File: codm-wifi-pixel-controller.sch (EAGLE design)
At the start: 20 parts, among them U1 ESP-WROOM-02, U2 AP2112K, U3 SN74AHCT125D

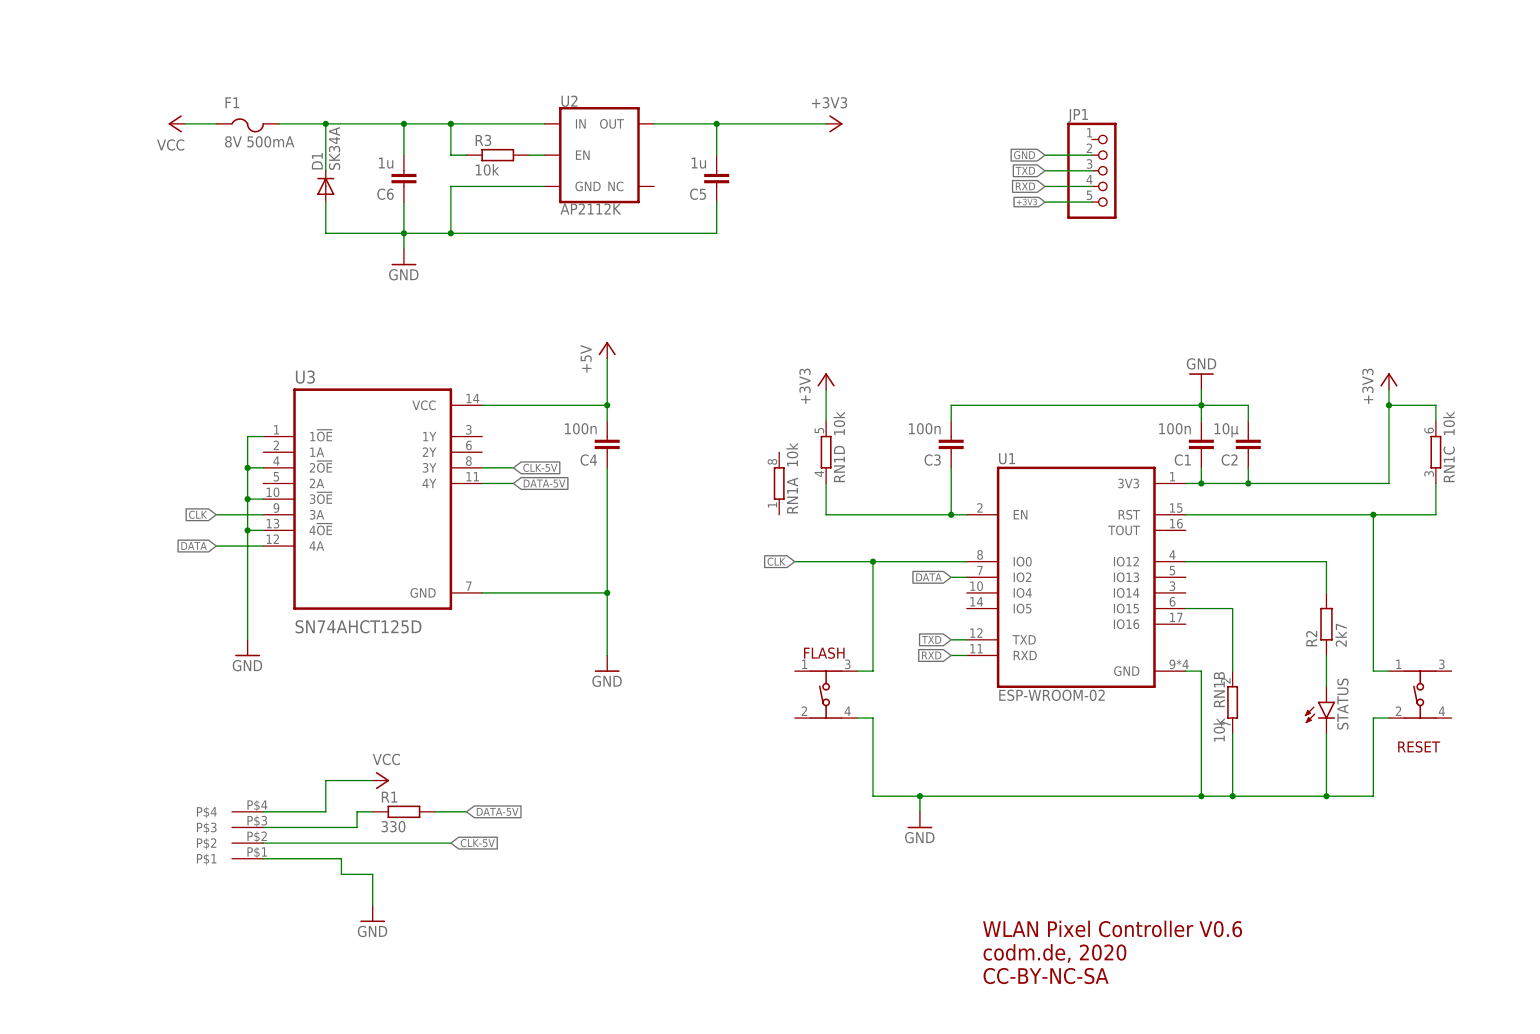
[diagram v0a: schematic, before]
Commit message: version with TLV767 and bigger thermal via/planes
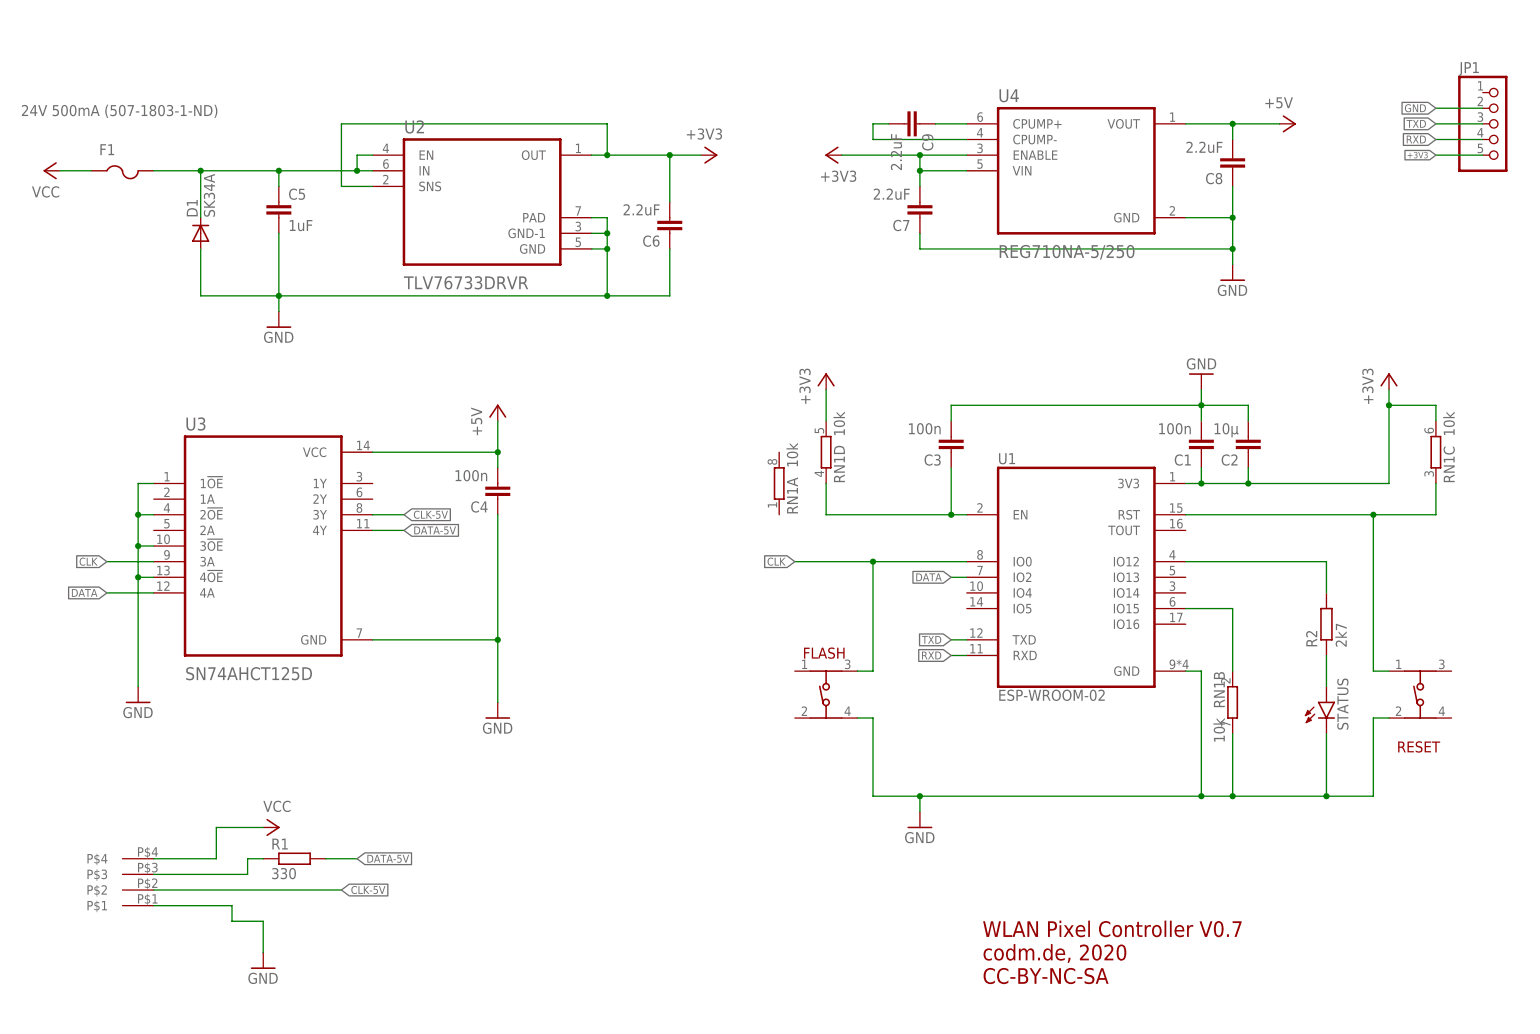
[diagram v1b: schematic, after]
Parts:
- removed R3: 10k, rcl:R-EU_R0805
- added C7, C8, C9: 2.2uF, rcl:C-EUC0603
- added U4: REG710NA-5/250, REG710NA-5_250:REG710NA-5/250
- C1, C2, C3, C4: device rcl:C-EUC0805 -> rcl:C-EUC0603
- C5: value 1u -> 1uF; device rcl:C-EUC0805 -> rcl:C-EUC0603
- C6: value 1u -> 2.2uF; device rcl:C-EUC0805 -> rcl:C-EUC0603
- F1: value 8V 500mA -> 24V 500mA (507-1803-1-ND)
- R1, R2: device rcl:R-EU_R0805 -> rcl:R-EU_R0603
- U2: value AP2112K -> TLV76733DRVR; device SparkFun-IC-Power:V_REG_AP2112K-3.3V -> TLV76733DRVR:TLV76733DRVR
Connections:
- new net N$3: C9.2, U4.CPUMP-
- new net VCCF: C5.1, D1.C, F1.2, U2.EN, U2.IN
- net +3V3: now also C6.2, C7.2, U2.SNS, U4.ENABLE, U4.VIN; no longer C5.2
- net +5V: now also C8.2, U4.VOUT; no longer C6.2, D1.C, F1.2, R3.1, U2.IN
- net GND: now also C5.2, C7.1, C8.1, U2.GND-1, U2.PAD, U4.GND; no longer C5.1
- net N$1: now also C9.1, U4.CPUMP+; no longer R3.2, U2.EN
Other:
- note added: "WLAN Pixel Controller V0.7 codm.de, 2020 CC-BY-NC-SA"
- note removed: "WLAN Pixel Controller V0.6 codm.de, 2020 CC-BY-NC-SA"
- moved on the sheet: C4, C5, C6, D1, F1, JP1, R1, U3

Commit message: prototype 0.7.2
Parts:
- added C10: 100n, rcl:C-EUC0603K
- added EN-2ND: (no value), jumper:SJ
- added R3: 330, rcl:R-EU_R0603
- added TP1, TP2, TP3, TP4, TP5, TP6, TP7, TP8, TP9: PTR1TP14R, testpad:PTR1TP14R
- C1, C2, C3, C7, C8, C9: device rcl:C-EUC0603 -> rcl:C-EUC0603K
- C4: value 100n -> 10u; device rcl:C-EUC0603 -> rcl:C-EUC0805
- C5: value 1uF -> 10uF/16V; device rcl:C-EUC0603 -> rcl:C-EUC0805K
- C6: value 2.2uF -> 100n; device rcl:C-EUC0603 -> rcl:C-EUC0603K
- U2: value TLV76733DRVR -> TLV1117LV33DCYR; device TLV76733DRVR:TLV76733DRVR -> TLV1117LV33DCYR:TLV1117LV33DCYR
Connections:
- net CLK-5V renamed CLK1-5V
- net DATA-5V renamed DATA1-5V
- new net CLK2-5V: TP9.TP, U3.1Y
- new net DATA2-5V: R3.2, U3.2Y
- new net DATA2-5VR: R3.1, TP8.TP
- new net IO13: TP5.TP, U1.IO13
- new net IO14: TP6.TP, U1.IO14
- new net IO16: U1.IO16, U3.1A
- new net IO4: TP3.TP, U1.IO4
- new net IO5: TP4.TP, U1.IO5
- new net N$4: EN-2ND.2, U3.1!OE, U3.2!OE
- net +3V3: now also C4.2, TP2.TP, U2.OUT_2, U2.OUT_4; no longer U2.OUT, U2.SNS
- net +5V: now also C10.2; no longer C4.2
- net GND: now also C10.1, EN-2ND.1, TP1.TP, TP7.TP; no longer U2.GND-1, U2.PAD, U3.1!OE, U3.2!OE
- net TXD: now also U3.2A
- net VCCF: no longer U2.EN
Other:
- note added: "478-3040-1-ND"
- moved on the sheet: C4, C6, RN1B

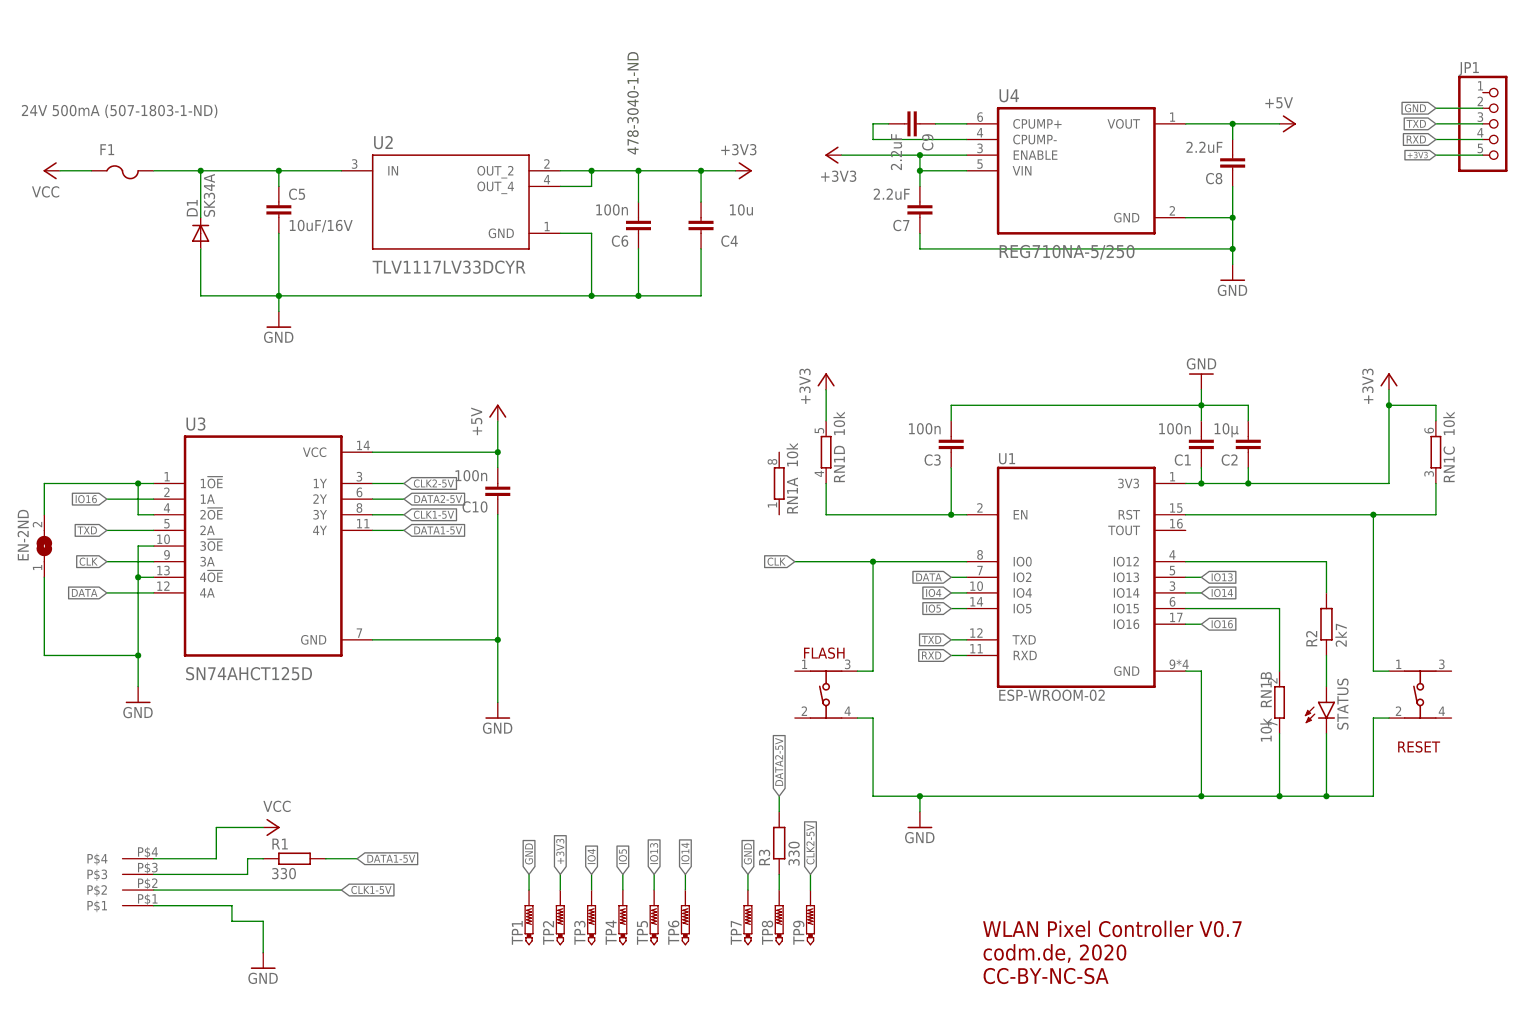
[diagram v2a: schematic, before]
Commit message: V0.7.3 - forgot reverse polarity protection
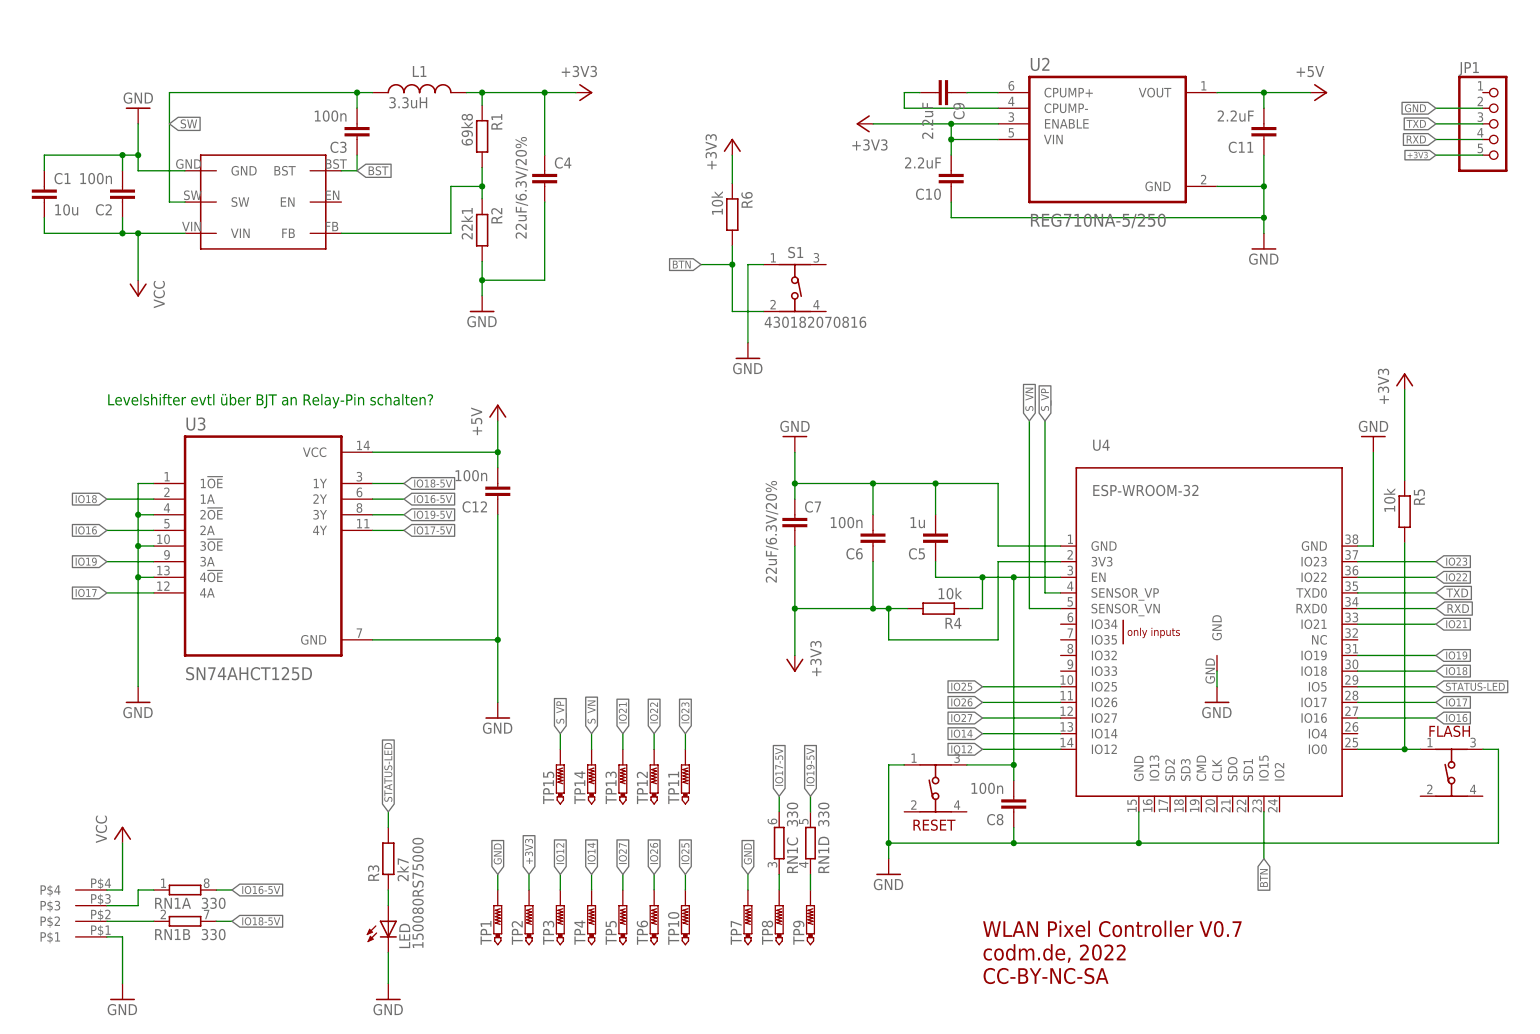
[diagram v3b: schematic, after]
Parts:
- removed D1: SK34A, diode:DIODE-DO214AC
- removed EN-2ND: (no value), jumper:SJ
- removed F1: 24V 500mA (507-1803-1-ND), adafruit:PTCFUSE-1206
- removed STATUS: (no value), led:LEDCHIPLED_0805
- added C11: 2.2uF, rcl:C-EUC0603K
- added C12: 100n, rcl:C-EUC0603K
- added L1: 3.3uH, Eagle_WE-LQ (rev19a):WE-LQ_1812_744045003
- added LED: 150080RS75000, led:LEDCHIP-LED0805
- added R4, R5, R6: 10k, rcl:R-EU_R0603
- added S1: 430182070816, Eagle_WS-TASV (rev21c):430182070816
- added TP10, TP11, TP12, TP13, TP14, TP15: PTR1TP14R, testpad:PTR1TP14R
- C1: value 100n -> 10u; device rcl:C-EUC0603K -> rcl:C-EUC0805K
- C10: value 100n -> 2.2uF
- C2: value 10µ -> 100n
- C4: value 10u -> 22uF/6.3V/20%; device rcl:C-EUC0805 -> rcl:C-EUC0805K
- C5: value 10uF/16V -> 1u; device rcl:C-EUC0805K -> rcl:C-EUC0603K
- C7: value 2.2uF -> 22uF/6.3V/20%; device rcl:C-EUC0603K -> rcl:C-EUC0805K
- C8: value 2.2uF -> 100n
- R1: value 330 -> 69k8
- R2: value 2k7 -> 22k1
- R3: value 330 -> 2k7
- RN1: value 10k -> 330
- U1: value ESP-WROOM-02 -> AP62XXX-TSOT26; device ESP-WROOM-02:ESP-WROOM-02 -> codm:AP62XXX-TSOT26
- U2: value TLV1117LV33DCYR -> REG710NA-5/250; device TLV1117LV33DCYR:TLV1117LV33DCYR -> REG710NA-5_250:REG710NA-5/250
- U4: value REG710NA-5/250 -> ESP-WROOM-32; device REG710NA-5_250:REG710NA-5/250 -> esp32:ESP-WROOM-32
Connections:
- removed net BOOTMODE: RN1B.1, U1.IO15
- removed net CHIPEN: C3.1, RN1D.1, U1.EN
- removed net CLK: FLASH.2, U1.IO0, U3.3A
- removed net CLK1-5V: U$101.P$2, U3.3Y
- removed net CLK2-5V: TP9.TP, U3.1Y
- removed net DATA: U1.IO2, U3.4A
- removed net DATA-5VR: R1.1, U$101.P$3
- removed net DATA1-5V: R1.2, U3.4Y
- removed net DATA2-5V: R3.2, U3.2Y
- removed net DATA2-5VR: R3.1, TP8.TP
- removed net IO13: TP5.TP, U1.IO13
- removed net IO4: TP3.TP, U1.IO4
- removed net IO5: TP4.TP, U1.IO5
- removed net N$1: C9.1, U4.CPUMP+
- removed net N$2: R2.1, STATUS.A
- removed net N$3: C9.2, U4.CPUMP-
- removed net N$4: EN-2ND.2, U3.1!OE, U3.2!OE
- removed net RST: RESET.1, RN1C.1, U1.RST
- removed net STATLED: R2.2, U1.IO12
- removed net VCCF: C5.1, D1.C, F1.2, U2.IN
- new net BST: C3.1, U1.BST
- new net BTN: R6.2, S1.2, U4.IO15
- new net GPIO0: FLASH.1, R5.2, U4.IO0
- new net IO12: TP3.TP, U4.IO12
- new net IO16-5V: RN1A.2, U3.2Y
- new net IO16-5VR: RN1A.1, U$101.P$3
- new net IO17: U3.4A, U4.IO17
- new net IO17-5V: RN1C.2, U3.4Y
- new net IO17-5VR: RN1C.1, TP8.TP
- new net IO18: U3.1A, U4.IO18
- new net IO18-5V: RN1B.2, U3.1Y
- new net IO18-5VR: RN1B.1, U$101.P$2
- new net IO19: U3.3A, U4.IO19
- new net IO19-5V: RN1D.2, U3.3Y
- new net IO19-5VR: RN1D.1, TP9.TP
- new net IO21: TP13.TP, U4.IO21
- new net IO22: TP12.TP, U4.IO22
- new net IO23: TP11.TP, U4.IO23
- new net IO25: TP10.TP, U4.IO25
- new net IO26: TP6.TP, U4.IO26
- new net IO27: TP5.TP, U4.IO27
- new net N$5: C9.1, U2.CPUMP+
- new net N$6: R1.2, R2.1, U1.FB
- new net N$7: LED.A, R3.1
- new net N$8: C9.2, U2.CPUMP-
- new net RESET: C5.1, C8.2, R4.1, RESET.2, U4.EN
- new net STATUS-LED: R3.2, U4.IO5
- new net SW: C3.2, L1.1, U1.SW
- new net S_VN: TP14.TP, U4.SENSOR_VN
- new net S_VP: TP15.TP, U4.SENSOR_VP
- net +3V3: now also C10.2, C4.1, C6.1, L1.2, R1.1, R4.2, R5.1, R6.1, U2.ENABLE, U2.VIN, U4.3V3; no longer C1.1, C2.1, C4.2, C6.2, RN1C.2, RN1D.2, U1.3V3, U2.OUT_2, U2.OUT_4, U4.ENABLE, U4.VIN
- net +5V: now also C11.2, C12.2, U2.VOUT; no longer C10.2, C8.2, U4.VOUT
- net GND: now also C1.1, C11.1, C12.1, C4.2, C6.2, FLASH.2, LED.C, R2.2, RESET.1, S1.1, U3.1!OE, U3.2!OE, U4.GND@1, U4.GND@15, U4.GND@38; no longer C1.2, C3.2, C4.1, C6.1, D1.A, EN-2ND.1, FLASH.4, RESET.3, RN1B.2, STATUS.C
- net IO14: now also TP4.TP, U4.IO14; no longer TP6.TP, U1.IO14
- net IO16: now also U3.2A, U4.IO16; no longer U1.IO16, U3.1A
- net RXD: now also U4.RXD0; no longer U1.RXD
- net TXD: now also U4.TXD0; no longer U1.TXD, U3.2A
- net VCC: now also C1.2, C2.1, U1.VIN; no longer F1.1
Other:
- note added: "Levelshifter evtl über BJT an Relay-Pin schalten?"
- note added: "WLAN Pixel Controller V0.7 codm.de, 2022 CC-BY-NC-SA"
- note removed: "478-3040-1-ND"
- note removed: "WLAN Pixel Controller V0.7 codm.de, 2020 CC-BY-NC-SA"
- moved on the sheet: C1, C10, C2, C3, C4, C5, C6, C7, C8, C9, FLASH, R1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
